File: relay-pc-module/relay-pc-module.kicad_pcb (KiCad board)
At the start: 2 copper layers, 75 x 75.1 mm, 61 parts, among them J1 Conn_02x02_Odd_Even, J10 Conn_01x01, J2 Conn_02x06_Odd_Even, J3 Conn_01x01, J4 Screw_Terminal_01x03, J5 Screw_Terminal_01x03, J6 Screw_Terminal_01x03, J7 Conn_01x04, J8 Conn_01x04, J9 Conn_01x01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

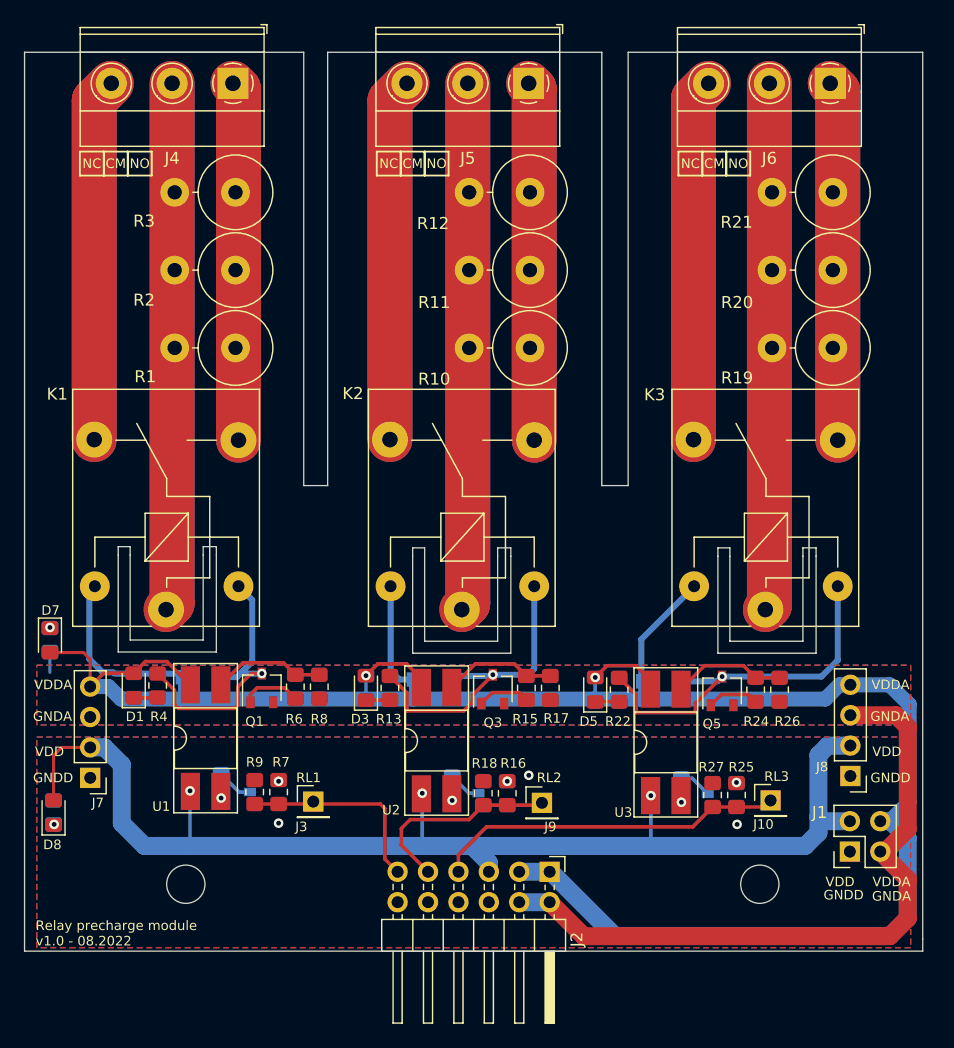
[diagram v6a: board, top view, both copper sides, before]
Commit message: Inverter relay module connector
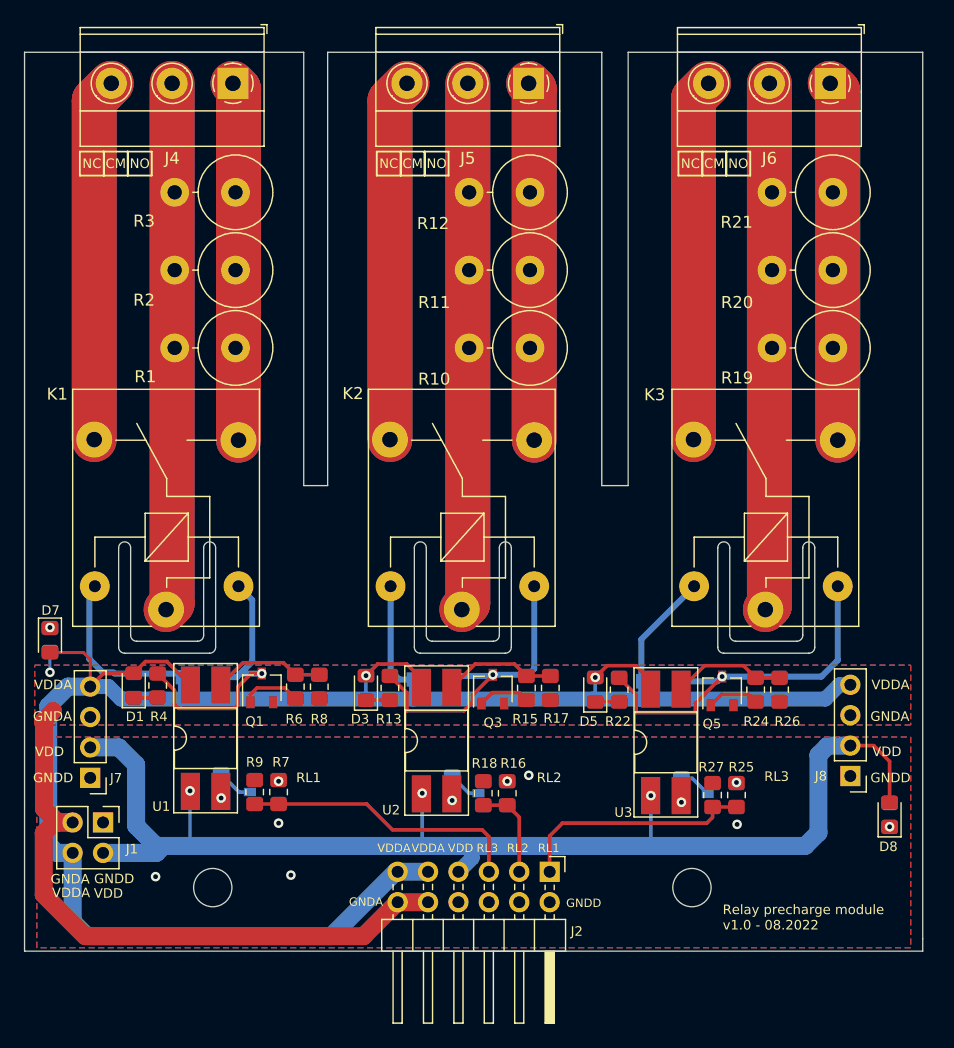
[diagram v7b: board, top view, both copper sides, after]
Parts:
- removed J10, J3, J9: Conn_01x01, Connector_PinHeader_2.54mm:PinHeader_1x01_P2.54mm_Vertical
- removed the REF** at (37.5, 92.2)
- removed the REF** at (85.4, 92.2)
- added REF**: MountingHole_3.2mm_M3, MountingHole:MountingHole_3.2mm_M3, F.Cu at (39.7, 92.5)
- added REF**: MountingHole_3.2mm_M3, MountingHole:MountingHole_3.2mm_M3, F.Cu at (79.7, 92.5)
- moved R29 69.8 mm to (96.2, 86.4)
- moved D8 69.8 mm to (96.2, 86.4)
- moved J1 62.4 mm to (30.5, 87.0), turned to -90 degrees
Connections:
- J2 pad 1: VDDA -> /RL3
- J2 pad 10: GNDD -> GNDA
- J2 pad 11: /RL1 -> VDDA
- J2 pad 12: GNDD -> GNDA
- J2 pad 2: GNDA -> GNDD
- J2 pad 3: VDDA -> /RL2
- J2 pad 4: GNDA -> GNDD
- J2 pad 5: VDD -> /RL1
- J2 pad 7: /RL3 -> VDD
- J2 pad 9: /RL2 -> VDDA
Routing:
- net /RL2: track 17.5 -> 7.98 mm
- net /RL3: track 29.4 -> 20.1 mm
- net /RL1: track 16.9 -> 23.6 mm
- net VDDA: track 196.9 -> 191.4 mm
- net GNDA: track 59.3 -> 55.7 mm, vias 0 -> 1
- net VDD: track 103.2 -> 105.8 mm
- net GNDD: vias 3 -> 5
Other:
- outline, holes or cut-outs redrawn
